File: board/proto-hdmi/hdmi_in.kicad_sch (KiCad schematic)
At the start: 43 parts, among them J2 HDMI_A

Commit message: Connect source port hotplug detect.
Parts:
- added U4: (no value), symbol 74xGxx:74LVC1G17
- C1: footprint Capacitor_SMD:C_0402_1005Metric -> (none)
- D1, D2: value (none) -> SBA0520Q; footprint (none) -> Diode_SMD:D_0402_1005Metric
- R21: value (none) -> 27k; footprint (none) -> Resistor_SMD:R_0402_1005Metric
- R22, R28: value (none) -> 10k; footprint (none) -> Resistor_SMD:R_0402_1005Metric
- R27: value (none) -> 47k; footprint (none) -> Resistor_SMD:R_0402_1005Metric
- R29: value (none) -> 1k; footprint (none) -> Resistor_SMD:R_0402_1005Metric
- SW1: value (none) -> CTS_218-4LPSTR; footprint (none) -> 0Local:CTS_218-4
- U1: footprint (none) -> Package_SON:X2SON-8_1.4x1mm_P0.35mm
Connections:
- net +3V3: now also U4.5 (VCC)
- net CEC: now also SW1.4
- net DETECT: now also U4.4
- net GND: now also U4.3 (GND)
- net HDMI_+5V: now also U4.2
- net CEC_THRU: now reaches SW1.5
- no-connect marks 3 -> 1
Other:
- note added: "CEC"
- note added: "CEC is a 3.3V bus, so it's connected directly to the FPGA."
- note added: "Hotplug Detection"
- note added: "Sink Connector"
- note added: "The DDC I^{2}C bus is connected to the FPGA through a level shifter when ENABLE is driven high. An EDID EEPROM can also optionally be connected to the bus. To write to the EEPROM turn on the write switch, connect an HDMI cable to a source port (including the one on this board), and write via the source DDC bus."
- note added: "The HPD line is driven high when ENABLE is high. This lets the FPGA simulate hotplug events. Alternatively, HPD can be tied to the HDMI +5V rail, which together with the EDID EEPROM allows a source to query EDID when the FPGA is off / ENABLE is low. The CEC bus can optionally be connected between the HDMI sink and source ports."
- moved on the sheet: C1, C2, C3, C4, C5, C6, D1, J2, R1, R10, R11, R12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

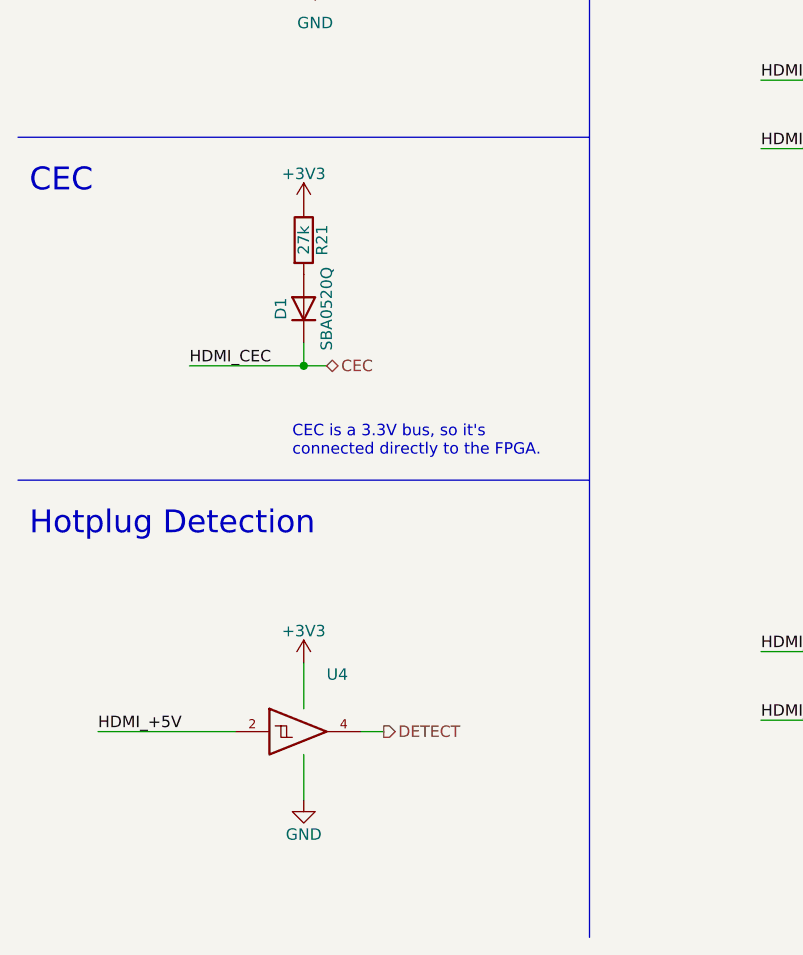
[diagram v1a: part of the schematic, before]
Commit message: Set up most of the non-TMDS source stuff.
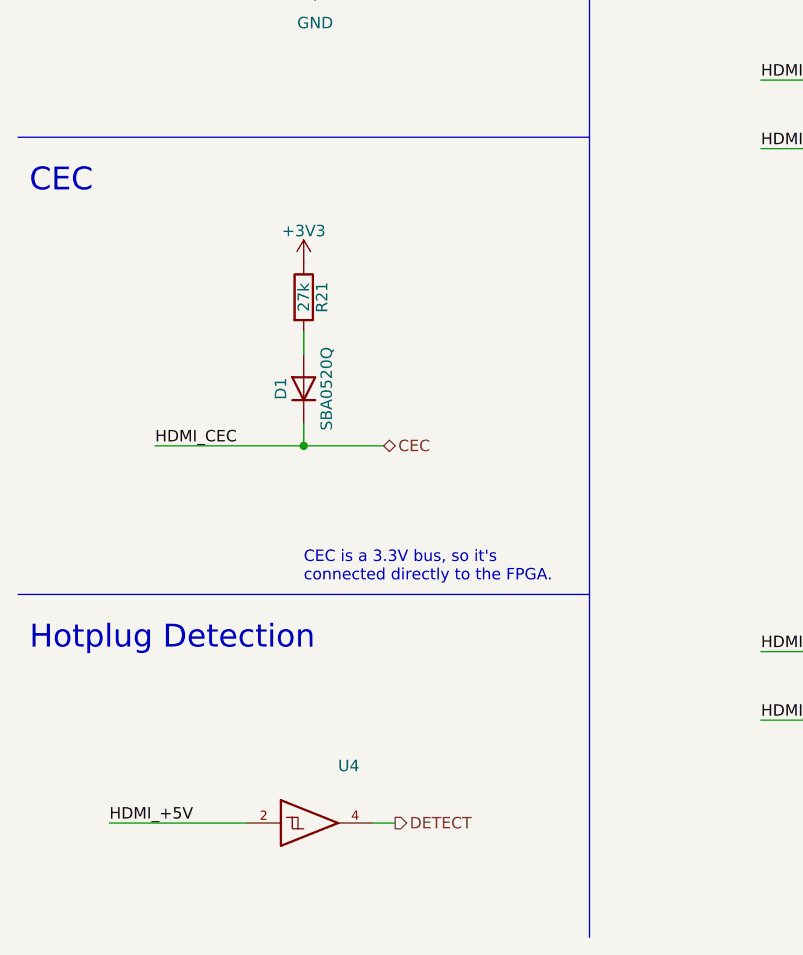
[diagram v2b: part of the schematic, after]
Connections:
- net +3V3: no longer U4.5 (VCC)
- new net VCC: U4.5 (VCC)
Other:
- moved on the sheet: D1, R21, U4
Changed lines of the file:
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@@
   (junction (at 218.44 26.67) (diameter 0) (color 0 0 0 0)
   )
-  (junction (at 44.45 139.7) (diameter 0) (color 0 0 0 0)
+  (junction (at 44.45 148.59) (diameter 0) (color 0 0 0 0)
   )
   (junction (at 129.54 107.95) (diameter 0) (color 0 0 0 0)
@@
     (stroke (width 0) (type default) (color 0 0 0 0))
   )
+  (wire (pts (xy 44.45 135.89) (xy 44.45 138.43))
+    (stroke (width 0) (type default) (color 0 0 0 0))
+  )
   (wire (pts (xy 139.7 115.57) (xy 146.05 115.57))
     (stroke (width 0) (type default) (color 0 0 0 0))
@@
     (stroke (width 0) (type default) (color 0 0 0 0))
   )
-  (wire (pts (xy 21.59 180.34) (xy 36.83 180.34))
+  (wire (pts (xy 22.86 190.5) (xy 38.1 190.5))
     (stroke (width 0) (type default) (color 0 0 0 0))
   )
@@
     (stroke (width 0) (type default) (color 0 0 0 0))
   )
-  (wire (pts (xy 31.75 139.7) (xy 44.45 139.7))
+  (wire (pts (xy 27.94 148.59) (xy 44.45 148.59))
     (stroke (width 0) (type default) (color 0 0 0 0))
   )
@@
     (stroke (width 0) (type default) (color 0 0 0 0))
   )
-  (wire (pts (xy 44.45 137.16) (xy 44.45 139.7))
+  (wire (pts (xy 44.45 146.05) (xy 44.45 148.59))
     (stroke (width 0) (type default) (color 0 0 0 0))
   )
@@
     (stroke (width 0) (type default) (color 0 0 0 0))
   )
-  (wire (pts (xy 50.8 180.34) (xy 53.34 180.34))
+  (wire (pts (xy 52.07 190.5) (xy 54.61 190.5))
     (stroke (width 0) (type default) (color 0 0 0 0))
   )
@@
     (stroke (width 0) (type default) (color 0 0 0 0))
   )
-  (wire (pts (xy 44.45 172.72) (xy 44.45 177.8))
-    (stroke (width 0) (type default) (color 0 0 0 0))
-  )
   (wire (pts (xy 50.8 55.88) (xy 63.5 55.88))
     (stroke (width 0) (type default) (color 0 0 0 0))
@@
     (stroke (width 0) (type default) (color 0 0 0 0))
   )
-  (wire (pts (xy 44.45 139.7) (xy 46.99 139.7))
+  (wire (pts (xy 44.45 148.59) (xy 53.34 148.59))
     (stroke (width 0) (type default) (color 0 0 0 0))
   )
@@
     (stroke (width 0) (type default) (color 0 0 0 0))
   )
-  (wire (pts (xy 44.45 182.88) (xy 44.45 187.96))
-    (stroke (width 0) (type default) (color 0 0 0 0))
-  )
   (wire (pts (xy 218.44 109.22) (xy 238.76 109.22))
     (stroke (width 0) (type default) (color 0 0 0 0))
@@
     (stroke (width 0) (type default) (color 0 0 0 0))
   )
-  (polyline (pts (xy 12.7 152.4) (xy 76.2 152.4))
+  (polyline (pts (xy 12.7 165.1) (xy 76.2 165.1))
     (stroke (width 0) (type default) (color 0 0 0 0))
   )
@@
   )
   (text "CEC is a 3.3V bus, so it's\nconnected directly to the FPGA."
-    (at 43.18 149.86 0)
+    (at 44.45 163.83 0)
     (effects (font (size 1.27 1.27)) (justify left bottom))
   )
@@
     (effects (font (size 1.27 1.27)) (justify left bottom))
   )
-  (text "Hotplug Detection" (at 13.97 158.75 0)
+  (text "Hotplug Detection" (at 13.97 171.45 0)
     (effects (font (size 2.54 2.54)) (justify left bottom))
   )
@@
     (effects (font (size 1.27 1.27)) (justify left bottom))
   )
-  (label "HDMI_CEC" (at 31.75 139.7 0)
+  (label "HDMI_CEC" (at 27.94 148.59 0)
     (effects (font (size 1.27 1.27)) (justify left bottom))
   )
@@
     (effects (font (size 1.27 1.27)) (justify right bottom))
   )
-  (label "HDMI_+5V" (at 21.59 180.34 0)
+  (label "HDMI_+5V" (at 22.86 190.5 0)
     (effects (font (size 1.27 1.27)) (justify left bottom))
   )
@@
     (effects (font (size 1.27 1.27)) (justify right))
   )
-  (hierarchical_label "CEC" (shape bidirectional) (at 46.99 139.7 0)
+  (hierarchical_label "CEC" (shape bidirectional) (at 53.34 148.59 0)
     (effects (font (size 1.27 1.27)) (justify left))
   )
@@
     (effects (font (size 1.27 1.27)) (justify left))
   )
-  (hierarchical_label "DETECT" (shape output) (at 53.34 180.34 0)
+  (hierarchical_label "DETECT" (shape output) (at 54.61 190.5 0)
     (effects (font (size 1.27 1.27)) (justify left))
   )
@@
     (pin "2")
   )
-  (symbol (lib_id "74xGxx:74LVC1G17") (at 44.45 180.34 0) (unit 1)
-    (in_bom yes) (on_board yes)
-    (property "Reference" "U4" (id 0) (at 46.99 173.99 0)
-      (effects (font (size 1.27 1.27)) (justify left))
-    )
-    (property "Value" "" (id 1) (at 46.99 176.53 0)
-      (effects (font (size 1.27 1.27)) (justify left))
-    )
-    (property "Footprint" "" (id 2) (at 44.45 180.34 0)
-      (effects (font (size 1.27 1.27)) hide)
-    )
-    (property "Datasheet" "http://www.ti.com/lit/sg/scyt129e/scyt129e.pdf" (id 3) (at 44.45 180.34 0)
+  (symbol (lib_id "74xGxx:74LVC1G17") (at 45.72 190.5 0) (unit 1)
+    (in_bom yes) (on_board yes)
+    (property "Reference" "U4" (id 0) (at 48.26 184.15 0)
+      (effects (font (size 1.27 1.27)) (justify left))
+    )
+    (property "Value" "" (id 1) (at 48.26 186.69 0)
+      (effects (font (size 1.27 1.27)) (justify left))
+    )
+    (property "Footprint" "" (id 2) (at 45.72 190.5 0)
+      (effects (font (size 1.27 1.27)) hide)
+    )
+    (property "Datasheet" "http://www.ti.com/lit/sg/scyt129e/scyt129e.pdf" (id 3) (at 45.72 190.5 0)
       (effects (font (size 1.27 1.27)) hide)
     )
@@
     (pin "1")
     (pin "2")
-  )
-  (symbol (lib_id "power:GND") (at 44.45 187.96 0) (unit 1)
-    (in_bom yes) (on_board yes)
-    (property "Reference" "#PWR0120" (id 0) (at 44.45 194.31 0)
-      (effects (font (size 1.27 1.27)) hide)
-    )
-    (property "Value" "GND" (id 1) (at 44.45 191.77 0))
-    (property "Footprint" "" (id 2) (at 44.45 187.96 0)
-      (effects (font (size 1.27 1.27)) hide)
-    )
-    (property "Datasheet" "" (id 3) (at 44.45 187.96 0)
-      (effects (font (size 1.27 1.27)) hide)
-    )
-    (pin "1")
   )
   (symbol (lib_id "Device:R") (at 111.76 52.07 90) (unit 1)
@@
     (pin "8")
   )
-  (symbol (lib_id "Device:R") (at 44.45 125.73 0) (unit 1)
-    (in_bom yes) (on_board yes)
-    (property "Reference" "R21" (id 0) (at 46.482 125.73 90))
-    (property "Value" "27k" (id 1) (at 44.45 125.73 90))
-    (property "Footprint" "Resistor_SMD:R_0402_1005Metric" (id 2) (at 42.672 125.73 90)
-      (effects (font (size 1.27 1.27)) hide)
-    )
-    (property "Datasheet" "~" (id 3) (at 44.45 125.73 0)
+  (symbol (lib_id "Device:R") (at 44.45 132.08 0) (unit 1)
+    (in_bom yes) (on_board yes)
+    (property "Reference" "R21" (id 0) (at 46.482 132.08 90))
+    (property "Value" "27k" (id 1) (at 44.45 132.08 90))
+    (property "Footprint" "Resistor_SMD:R_0402_1005Metric" (id 2) (at 42.672 132.08 90)
+      (effects (font (size 1.27 1.27)) hide)
+    )
+    (property "Datasheet" "~" (id 3) (at 44.45 132.08 0)
       (effects (font (size 1.27 1.27)) hide)
     )
@@
     (pin "2")
   )
-  (symbol (lib_id "power:+3V3") (at 44.45 172.72 0) (unit 1)
-    (in_bom yes) (on_board yes)
-    (property "Reference" "#PWR0117" (id 0) (at 44.45 176.53 0)
-      (effects (font (size 1.27 1.27)) hide)
-    )
-    (property "Value" "+3V3" (id 1) (at 44.45 169.164 0))
-    (property "Footprint" "" (id 2) (at 44.45 172.72 0)
-      (effects (font (size 1.27 1.27)) hide)
-    )
-    (property "Datasheet" "" (id 3) (at 44.45 172.72 0)
-      (effects (font (size 1.27 1.27)) hide)
-    )
-    (pin "1")
-  )
   (symbol (lib_id "Device:C") (at 123.19 171.45 90) (unit 1)
     (in_bom yes) (on_board yes)
@@
     (pin "2")
   )
-  (symbol (lib_id "power:+3V3") (at 44.45 121.92 0) (unit 1)
-    (in_bom yes) (on_board yes)
-    (property "Reference" "#PWR01" (id 0) (at 44.45 125.73 0)
-      (effects (font (size 1.27 1.27)) hide)
-    )
-    (property "Value" "+3V3" (id 1) (at 44.45 118.364 0))
-    (property "Footprint" "" (id 2) (at 44.45 121.92 0)
-      (effects (font (size 1.27 1.27)) hide)
-    )
-    (property "Datasheet" "" (id 3) (at 44.45 121.92 0)
+  (symbol (lib_id "power:+3V3") (at 44.45 128.27 0) (unit 1)
+    (in_bom yes) (on_board yes)
+    (property "Reference" "#PWR01" (id 0) (at 44.45 132.08 0)
+      (effects (font (size 1.27 1.27)) hide)
+    )
+    (property "Value" "+3V3" (id 1) (at 44.45 124.714 0))
+    (property "Footprint" "" (id 2) (at 44.45 128.27 0)
+      (effects (font (size 1.27 1.27)) hide)
+    )
+    (property "Datasheet" "" (id 3) (at 44.45 128.27 0)
       (effects (font (size 1.27 1.27)) hide)
     )
@@
     (pin "1")
   )
-  (symbol (lib_id "Device:D") (at 44.45 133.35 90) (unit 1)
-    (in_bom yes) (on_board yes)
-    (property "Reference" "D1" (id 0) (at 41.91 133.35 0))
-    (property "Value" "SBA0520Q" (id 1) (at 46.99 133.35 0))
-    (property "Footprint" "Diode_SMD:D_0402_1005Metric" (id 2) (at 44.45 133.35 0)
-      (effects (font (size 1.27 1.27)) hide)
-    )
-    (property "Datasheet" "~" (id 3) (at 44.45 133.35 0)
-      (effects (font (size 1.27 1.27)) hide)
-    )
+  (symbol (lib_id "Device:D") (at 44.45 142.24 90) (unit 1)
+    (in_bom yes) (on_board yes)
+    (property "Reference" "D1" (id 0) (at 41.91 142.24 0))
+    (property "Value" "SBA0520Q" (id 1) (at 46.99 142.24 0))
+    (property "Footprint" "Diode_SMD:D_0402_1005Metric" (id 2) (at 44.45 142.24 0)
+      (effects (font (size 1.27 1.27)) hide)
+    )
+    (property "Datasheet" "~" (id 3) (at 44.45 142.24 0)
+      (effects (font (size 1.27 1.27)) hide)
+    )

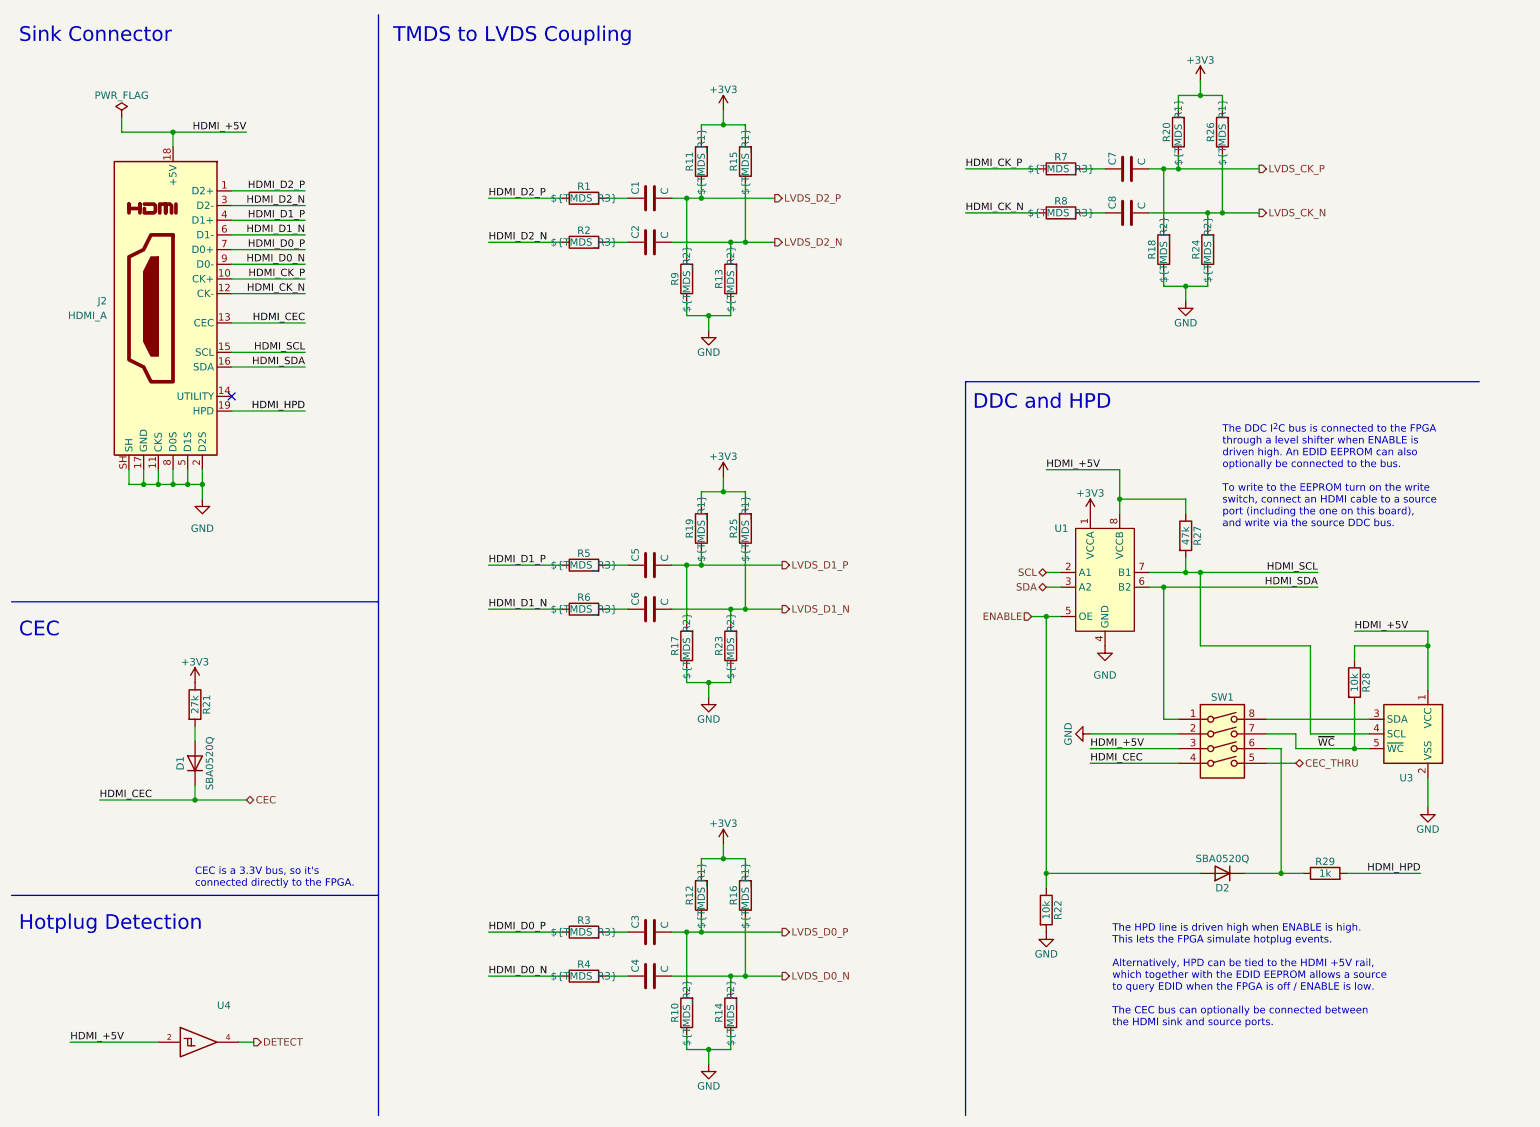
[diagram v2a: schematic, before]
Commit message: Fix DRC issues on HDMI board.
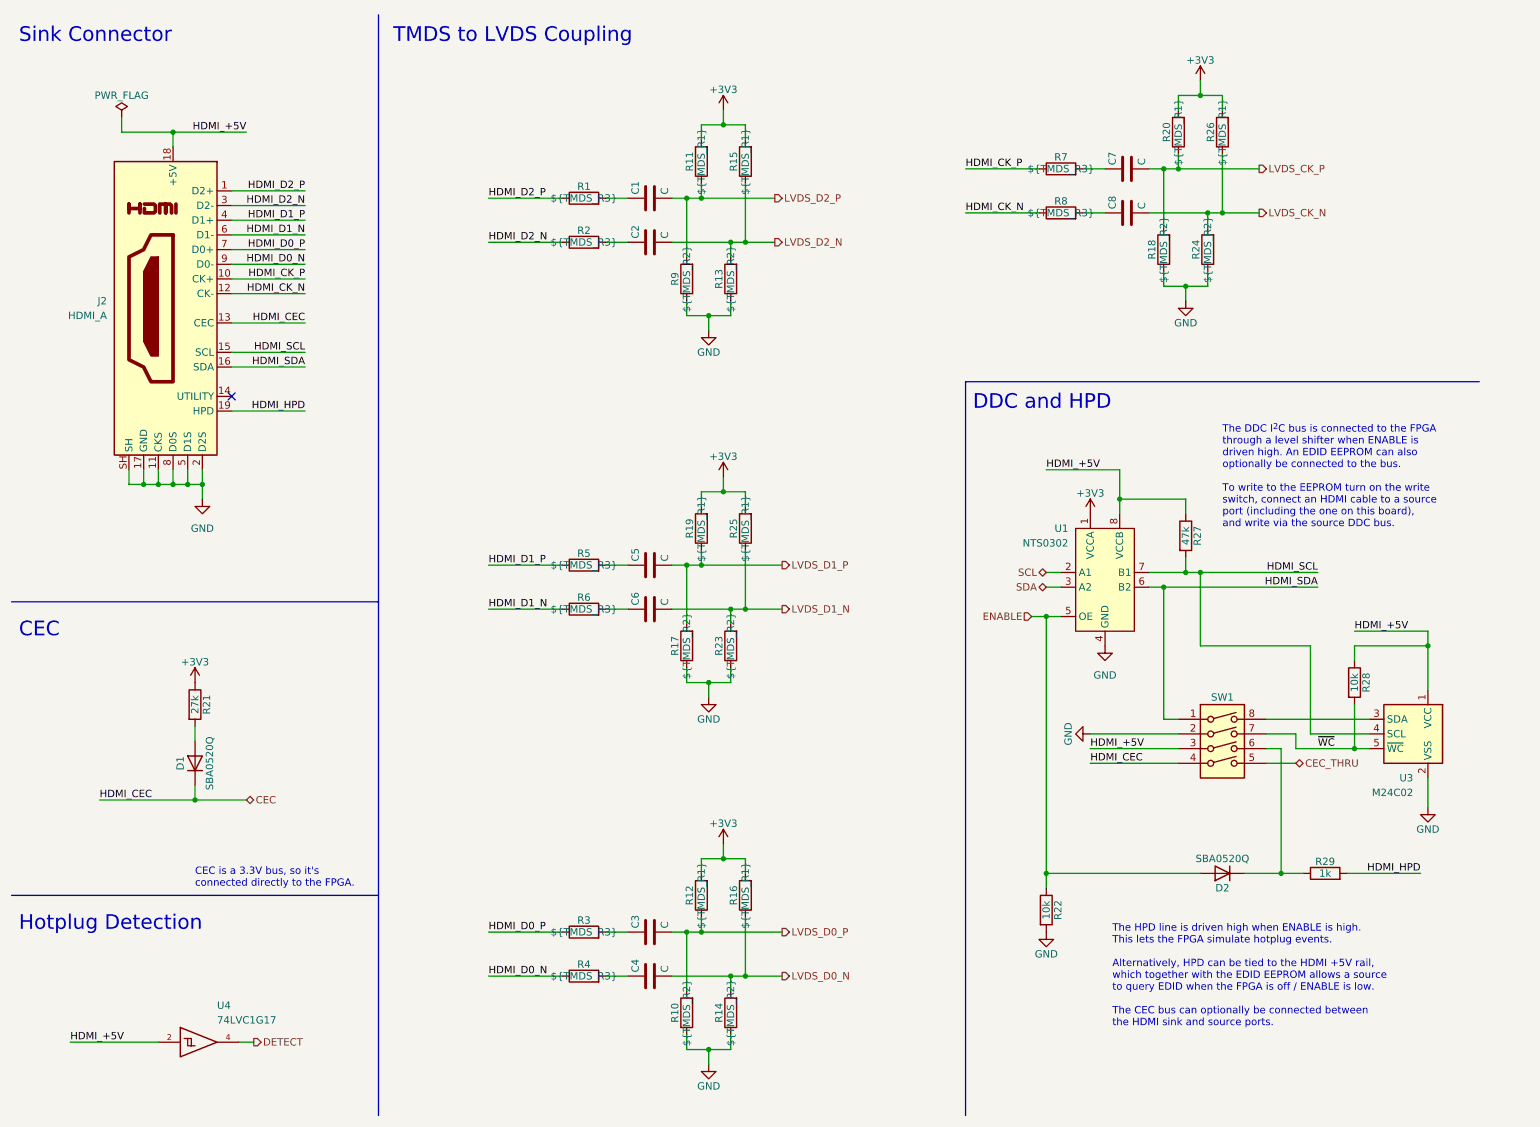
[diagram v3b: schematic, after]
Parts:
- C1: footprint (none) -> Capacitor_SMD:C_0402_1005Metric
- U1: value (none) -> NTS0302
- U3: value (none) -> M24C02
- U4: value (none) -> 74LVC1G17; footprint (none) -> Package_TO_SOT_SMD:SOT-886
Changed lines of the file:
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@@
       (effects (font (size 1.27 1.27)) (justify left))
     )
-    (property "Value" "" (id 1) (at 48.26 186.69 0)
-      (effects (font (size 1.27 1.27)) (justify left))
-    )
-    (property "Footprint" "" (id 2) (at 45.72 190.5 0)
+    (property "Value" "74LVC1G17" (id 1) (at 48.26 186.69 0)
+      (effects (font (size 1.27 1.27)) (justify left))
+    )
+    (property "Footprint" "Package_TO_SOT_SMD:SOT-886" (id 2) (at 45.72 190.5 0)
       (effects (font (size 1.27 1.27)) hide)
     )
@@
       (effects (font (size 1.27 1.27)) (justify left))
     )
-    (property "Value" "" (id 1) (at 255.27 147.32 0)
+    (property "Value" "M24C02" (id 1) (at 255.27 147.32 0)
       (effects (font (size 1.27 1.27)) (justify left))
     )
@@
       (effects (font (size 1.27 1.27)) (justify left))
     )
-    (property "Footprint" "" (id 2) (at 127 43.4848 0)
+    (property "Footprint" "Capacitor_SMD:C_0402_1005Metric" (id 2) (at 127 43.4848 0)
       (effects (font (size 1.27 1.27)) hide)
     )
@@
       (effects (font (size 1.27 1.27)) (justify right))
     )
-    (property "Value" "" (id 1) (at 195.58 104.14 0)
+    (property "Value" "NTS0302" (id 1) (at 195.58 104.14 0)
       (effects (font (size 1.27 1.27)) (justify right))
     )
